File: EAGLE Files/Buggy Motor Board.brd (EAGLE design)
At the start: 100 x 80 mm, 50 parts, among them CON0 M025MM, CON1 M025MM, IC4 4050D, IC5 LP298XS, U1 MCP2551, X1 MICROSD, X2 5566-24, X3 5566-24, Y2 16MHZ

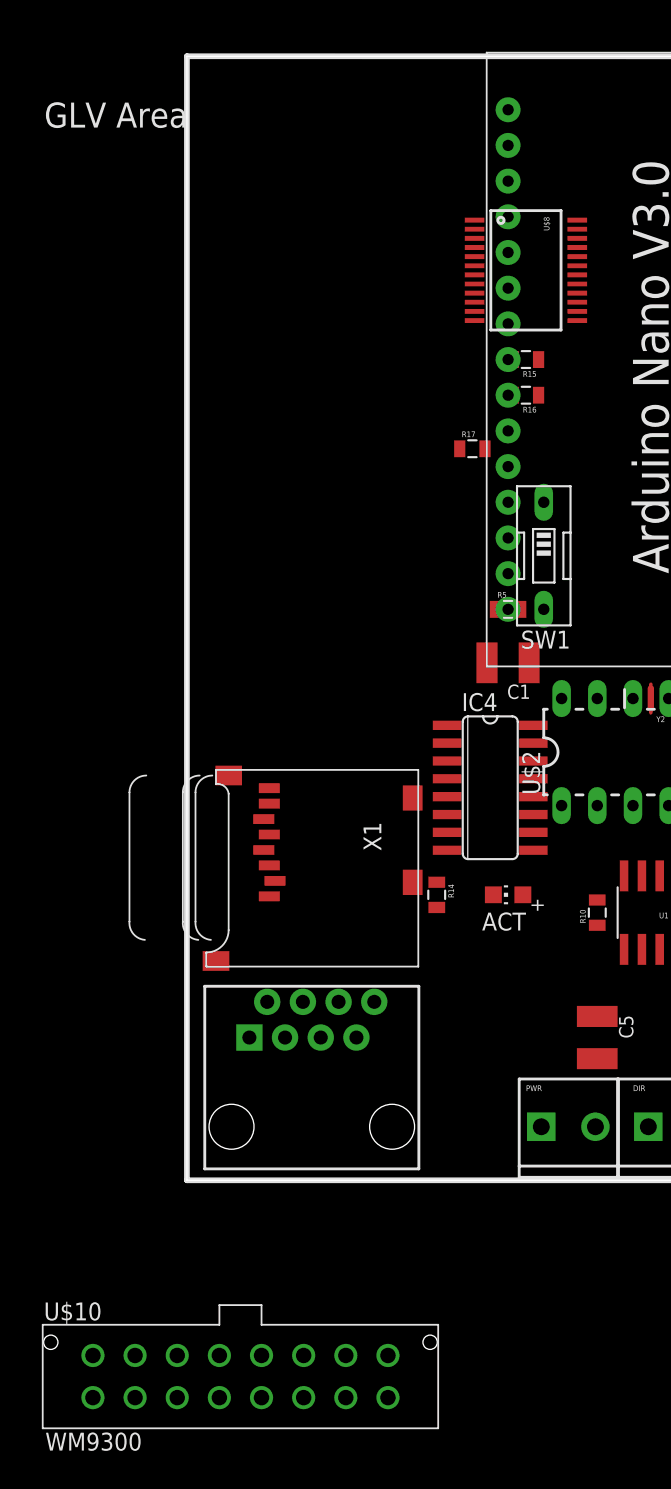
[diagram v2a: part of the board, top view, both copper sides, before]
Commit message: 5v Optocoupling
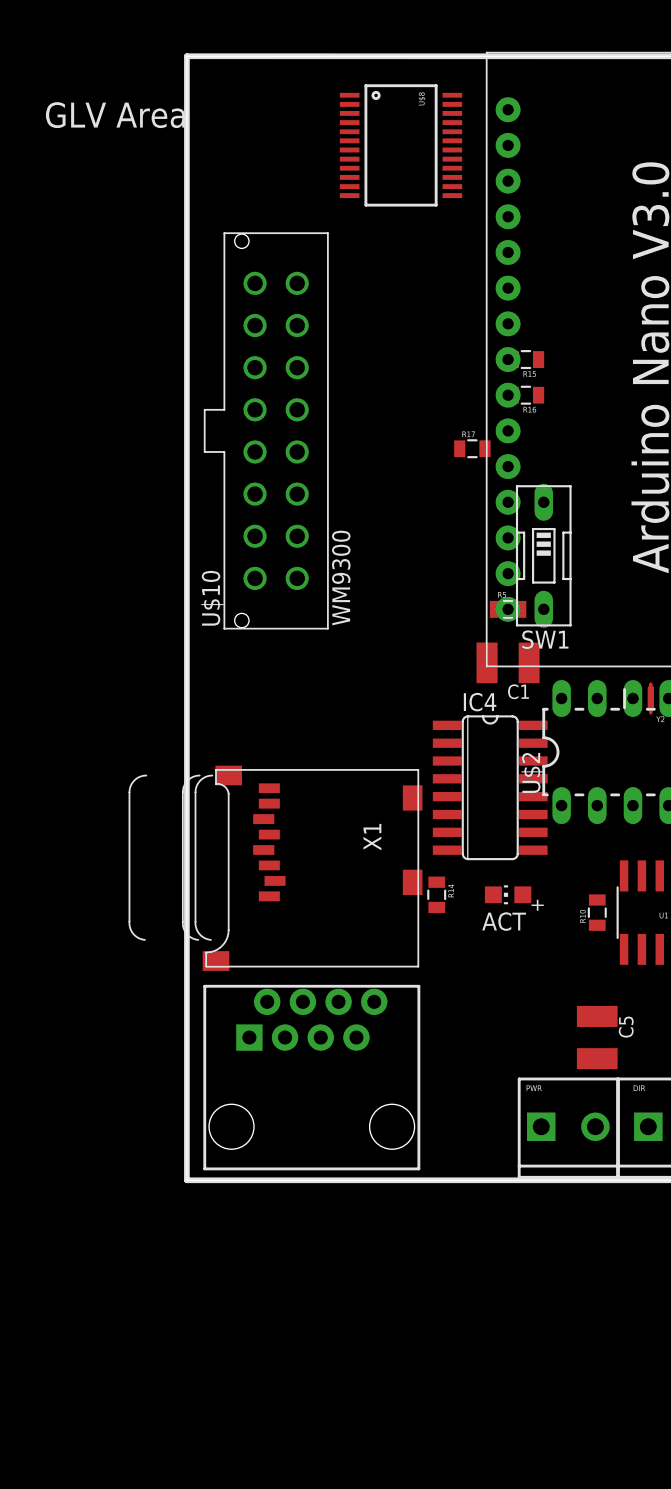
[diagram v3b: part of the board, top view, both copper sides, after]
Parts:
- moved U$10 67.4 mm to (6.35, 53.3), turned to 90 degrees
- moved U$8 12.6 mm to (15.2, 73.7)
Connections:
- net +12V: no longer R12.2, R13.2, R5.2, R6.2, R7.2
- net +5V: now also R12.2, R13.2, R5.2, R6.2, R7.2
- net OPTO0: now also U$1.D7
- net OPTO1: now also U$1.D6*
- net OPTO2: now also U$1.D5*
- net OPTO3: now also U$1.D4
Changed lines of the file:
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@@
 <element name="U$4" library="SparkFun-AnalogIC" package="SOT23-6-MCP4725" value="DAC_MCP4725SOT-CP" x="67.31" y="36.83" rot="R90"/>
 <element name="U$5" library="SparkFun-Connectors" package="RJ45-8" value="RJ45-8PTH" x="8.89" y="3.81"/>
-<element name="U$8" library="SparkFun-AnalogIC" package="SSOP24" value="MUX-74HC4067SMD" x="24.13" y="64.77" rot="R270"/>
+<element name="U$8" library="SparkFun-AnalogIC" package="SSOP24" value="MUX-74HC4067SMD" x="15.24" y="73.66" rot="R270"/>
 <element name="U1" library="SparkFun-DigitalIC" package="SO08" value="MCP2551" x="33.02" y="19.05" rot="R180"/>
 <element name="X1" library="adafruit" package="MICROSD" value="MICROSD" x="16.51" y="29.21" rot="R270"/>
@@
 <element name="C4" library="rcl" package="C1210K" value="" x="62.23" y="45.72"/>
 <element name="C5" library="rcl" package="C1210K" value="" x="29.21" y="10.16" rot="R270"/>
-<element name="U$10" library="Wetmelon-Connectors" package="WM9300" value="WM9300" x="3.81" y="-13.97"/>
+<element name="U$10" library="Wetmelon-Connectors" package="WM9300" value="WM9300" x="6.35" y="53.34" rot="R90"/>
 </elements>
 <signals>
@@
 <wire x1="2.97" y1="28.81" x2="5.47" y2="25.71" width="0" layer="19" extent="1-1"/>
 <wire x1="19.42" y1="52.07" x2="22.86" y2="43.18" width="0" layer="19" extent="1-1"/>
-<wire x1="20.474" y1="61.195" x2="19.42" y2="52.07" width="0" layer="19" extent="1-1"/>
+<wire x1="11.584" y1="70.085" x2="19.42" y2="52.07" width="0" layer="19" extent="1-1"/>
 </signal>
 <signal name="MODE1">
@@
 <vertex x="0" y="0"/>
 </polygon>
+<contactref element="R5" pad="2"/>
+<contactref element="R7" pad="2"/>
+<contactref element="R13" pad="2"/>
+<contactref element="R12" pad="2"/>
+<contactref element="R6" pad="2"/>
+<wire x1="49.9" y1="57.15" x2="49.9" y2="59.69" width="0" layer="19" extent="1-1"/>
+<wire x1="49.9" y1="54.61" x2="49.9" y2="57.15" width="0" layer="19" extent="1-1"/>
+<wire x1="49.9" y1="52.07" x2="49.9" y2="54.61" width="0" layer="19" extent="1-1"/>
+<wire x1="53.2638" y1="42.545" x2="49.9" y2="52.07" width="0" layer="19" extent="1-1"/>
+<wire x1="46.99" y1="34.29" x2="53.2638" y2="42.545" width="0" layer="19" extent="1-1"/>
+<wire x1="52.07" y1="31.75" x2="46.99" y2="34.29" width="0" layer="19" extent="1-1"/>
+<wire x1="32.385" y1="21.6662" x2="46.99" y2="34.29" width="0" layer="19" extent="1-1"/>
+<wire x1="29.21" y1="18.15" x2="32.385" y2="21.6662" width="0" layer="19" extent="1-1"/>
+<wire x1="29.21" y1="11.66" x2="29.21" y2="18.15" width="0" layer="19" extent="1-1"/>
+<wire x1="37.15" y1="13.94" x2="29.21" y2="11.66" width="0" layer="19" extent="1-1"/>
+<wire x1="39.05" y1="13.94" x2="37.15" y2="13.94" width="0" layer="19" extent="1-1"/>
+<wire x1="23.76" y1="40.64" x2="32.385" y2="21.6662" width="0" layer="19" extent="1-1"/>
+<wire x1="22.86" y1="48.26" x2="23.76" y2="40.64" width="0" layer="19" extent="1-1"/>
+<wire x1="23.23" y1="55.88" x2="22.86" y2="48.26" width="0" layer="19" extent="1-1"/>
+<wire x1="23.23" y1="58.42" x2="23.23" y2="55.88" width="0" layer="19" extent="1-1"/>
+<wire x1="18.896" y1="77.235" x2="23.23" y2="58.42" width="0" layer="19" extent="1-1"/>
 </signal>
 <signal name="SCK">
@@
 <contactref element="U$8" pad="1"/>
 <contactref element="U$1" pad="A6"/>
-<wire x1="22.86" y1="53.34" x2="20.474" y2="68.345" width="0" layer="19" extent="1-1"/>
+<wire x1="22.86" y1="53.34" x2="11.584" y2="77.235" width="0" layer="19" extent="1-1"/>
 </signal>
 <signal name="AMUX0">
 <contactref element="U$8" pad="10"/>
 <contactref element="U$1" pad="A0"/>
-<wire x1="20.474" y1="62.495" x2="22.86" y2="68.58" width="0" layer="19" extent="1-1"/>
+<wire x1="11.584" y1="71.385" x2="22.86" y2="68.58" width="0" layer="19" extent="1-1"/>
 </signal>
 <signal name="AMUX1">
 <contactref element="U$8" pad="11"/>
 <contactref element="U$1" pad="A1"/>
-<wire x1="20.474" y1="61.845" x2="22.86" y2="66.04" width="0" layer="19" extent="1-1"/>
+<wire x1="11.584" y1="70.735" x2="22.86" y2="66.04" width="0" layer="19" extent="1-1"/>
 </signal>
 <signal name="AMUX2">
 <contactref element="U$8" pad="14"/>
 <contactref element="U$1" pad="A2"/>
-<wire x1="27.786" y1="61.845" x2="22.86" y2="63.5" width="0" layer="19" extent="1-1"/>
+<wire x1="18.896" y1="70.735" x2="22.86" y2="63.5" width="0" layer="19" extent="1-1"/>
 </signal>
 <signal name="AMUX3">
 <contactref element="U$8" pad="13"/>
 <contactref element="U$1" pad="A3"/>
-<wire x1="27.786" y1="61.195" x2="22.86" y2="60.96" width="0" layer="19" extent="1-1"/>
+<wire x1="18.896" y1="70.085" x2="22.86" y2="60.96" width="0" layer="19" extent="1-1"/>
 </signal>
 <signal name="N$23">
@@
 <contactref element="U$8" pad="15"/>
 <contactref element="R17" pad="2"/>
-<wire x1="21.22" y1="52.07" x2="27.786" y2="62.495" width="0" layer="19" extent="1-1"/>
+<wire x1="21.22" y1="52.07" x2="18.896" y2="71.385" width="0" layer="19" extent="1-1"/>
 </signal>
 <signal name="+12V">
 <contactref element="C1" pad="1"/>
-<contactref element="R5" pad="2"/>
 <contactref element="U$1" pad="VIN"/>
 <contactref element="PWR" pad="2"/>
-<contactref element="R6" pad="2"/>
-<contactref element="R7" pad="2"/>
-<contactref element="R12" pad="2"/>
-<contactref element="R13" pad="2"/>
-<wire x1="49.9" y1="57.15" x2="49.9" y2="59.69" width="0" layer="19" extent="1-1"/>
-<wire x1="49.9" y1="54.61" x2="49.9" y2="57.15" width="0" layer="19" extent="1-1"/>
-<wire x1="49.9" y1="52.07" x2="49.9" y2="54.61" width="0" layer="19" extent="1-1"/>
-<wire x1="22.86" y1="40.64" x2="49.9" y2="52.07" width="0" layer="19" extent="1-1"/>
-<wire x1="23.76" y1="40.64" x2="22.86" y2="40.64" width="0" layer="19" extent="1-1"/>
-<wire x1="24.36" y1="36.83" x2="23.76" y2="40.64" width="0" layer="19" extent="1-1"/>
+<wire x1="24.36" y1="36.83" x2="22.86" y2="40.64" width="0" layer="19" extent="1-1"/>
 <wire x1="29.0778" y1="3.81" x2="24.36" y2="36.83" width="0" layer="19" extent="1-1"/>
 </signal>
@@
 <contactref element="MODES" pad="3"/>
 <contactref element="U$6" pad="2"/>
+<contactref element="U$1" pad="D7"/>
+<wire x1="38.1" y1="63.5" x2="54.15" y2="58.42" width="0" layer="19" extent="1-1"/>
 <wire x1="51.6278" y1="3.81" x2="54.15" y2="58.42" width="0" layer="19" extent="1-1"/>
 </signal>
@@
 <contactref element="MODES" pad="2"/>
 <contactref element="U$6" pad="4"/>
+<contactref element="U$1" pad="D6*"/>
+<wire x1="38.1" y1="60.96" x2="54.15" y2="55.88" width="0" layer="19" extent="1-1"/>
 <wire x1="47.95" y1="3.81" x2="54.15" y2="55.88" width="0" layer="19" extent="1-1"/>
 </signal>
@@
 <contactref element="DIR" pad="3"/>
 <contactref element="U$6" pad="6"/>
+<contactref element="U$1" pad="D5*"/>
+<wire x1="38.1" y1="58.42" x2="54.15" y2="53.34" width="0" layer="19" extent="1-1"/>
 <wire x1="40.1978" y1="3.81" x2="54.15" y2="53.34" width="0" layer="19" extent="1-1"/>
 </signal>
@@
 <contactref element="DIR" pad="2"/>
 <contactref element="U$6" pad="8"/>
+<contactref element="U$1" pad="D4"/>
+<wire x1="38.1" y1="55.88" x2="54.15" y2="50.8" width="0" layer="19" extent="1-1"/>
 <wire x1="36.52" y1="3.81" x2="54.15" y2="50.8" width="0" layer="19" extent="1-1"/>
 </signal>
